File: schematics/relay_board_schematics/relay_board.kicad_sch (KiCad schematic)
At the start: 42 parts, among them J1 Programming Header, P1 ACT_PWR, P2 ACT_PWR, P3 ACTUATOR, Q1 MMBF170, Q2 MMBF170, SW1 SW_DIP_x04, U1 SPST_POWER_RELAY, U2 PIC16F1826-ISO, U3 dpdt_relay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

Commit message: clean up on project files naming except symbol lib
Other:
- title: RLCS Relay_Board -> RLCS Relay Board
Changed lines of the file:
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@@
   (paper "A4")
   (title_block
-    (title "RLCS Relay_Board")
+    (title "RLCS Relay Board")
     (date "2022-11-25")
     (rev "A")

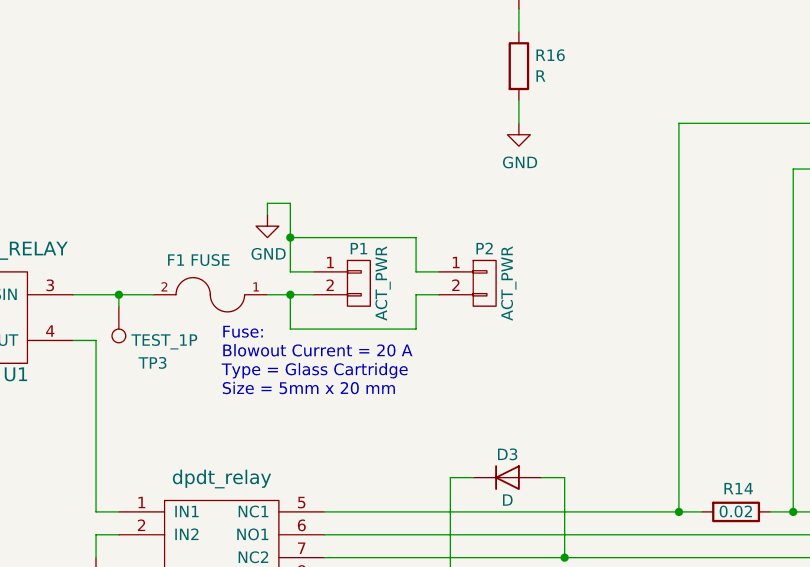
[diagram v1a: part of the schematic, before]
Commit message: reverse pinout on P2 connector
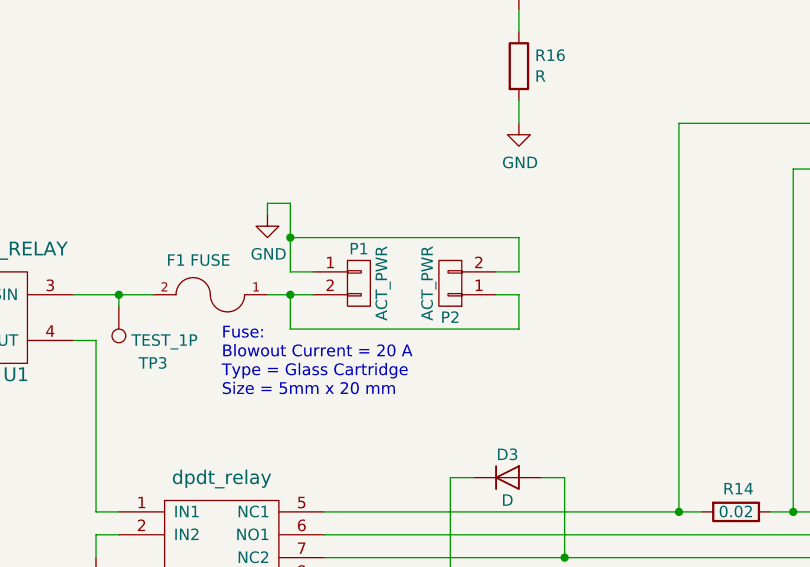
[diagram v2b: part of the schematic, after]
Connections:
- net GND: now also P2.2 (P2); no longer P2.1 (P1)
- net at F1.1, P1.2 (P2): now also P2.1 (P1); no longer P2.2 (P2)
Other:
- moved on the sheet: P2
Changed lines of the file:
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@@
-    (stroke (width 0) (type default) (color 0 0 0 0))
-  )
-  (wire (pts (xy 158.75 120.65) (xy 172.72 120.65))
     (stroke (width 0) (type default) (color 0 0 0 0))
   )
@@
     (stroke (width 0) (type default) (color 0 0 0 0))
   )
+  (wire (pts (xy 184.15 116.84) (xy 181.61 116.84))
+    (stroke (width 0) (type default) (color 0 0 0 0))
+  )
   (wire (pts (xy 218.44 119.38) (xy 233.68 119.38))
     (stroke (width 0) (type default) (color 0 0 0 0))
@@
     (stroke (width 0) (type default) (color 0 0 0 0))
   )
+  (wire (pts (xy 158.75 120.65) (xy 184.15 120.65))
+    (stroke (width 0) (type default) (color 0 0 0 0))
+  )
   (wire (pts (xy 48.006 35.814) (xy 48.006 39.37))
     (stroke (width 0) (type default) (color 0 0 0 0))
@@
     (stroke (width 0) (type default) (color 0 0 0 0))
   )
-  (wire (pts (xy 172.72 116.84) (xy 172.72 120.65))
-    (stroke (width 0) (type default) (color 0 0 0 0))
-  )
   (wire (pts (xy 73.66 86.36) (xy 71.12 86.36))
     (stroke (width 0) (type default) (color 0 0 0 0))
@@
     (stroke (width 0) (type default) (color 0 0 0 0))
   )
+  (wire (pts (xy 184.15 110.49) (xy 184.15 114.3))
+    (stroke (width 0) (type default) (color 0 0 0 0))
+  )
   (wire (pts (xy 212.09 140.97) (xy 214.63 140.97))
     (stroke (width 0) (type default) (color 0 0 0 0))
@@
     (stroke (width 0) (type default) (color 0 0 0 0))
   )
-  (wire (pts (xy 175.26 114.3) (xy 172.72 114.3))
-    (stroke (width 0) (type default) (color 0 0 0 0))
-  )
   (wire (pts (xy 194.31 25.4) (xy 194.31 26.67))
     (stroke (width 0) (type default) (color 0 0 0 0))
@@
     (stroke (width 0) (type default) (color 0 0 0 0))
   )
+  (wire (pts (xy 184.15 120.65) (xy 184.15 116.84))
+    (stroke (width 0) (type default) (color 0 0 0 0))
+  )
   (wire (pts (xy 119.38 186.69) (xy 119.38 184.15))
     (stroke (width 0) (type default) (color 0 0 0 0))
@@
     (stroke (width 0) (type default) (color 0 0 0 0))
   )
+  (wire (pts (xy 184.15 114.3) (xy 181.61 114.3))
+    (stroke (width 0) (type default) (color 0 0 0 0))
+  )
   (wire (pts (xy 201.93 97.79) (xy 201.93 140.97))
     (stroke (width 0) (type default) (color 0 0 0 0))
@@
     (stroke (width 0) (type default) (color 0 0 0 0))
   )
-  (wire (pts (xy 158.75 110.49) (xy 172.72 110.49))
+  (wire (pts (xy 158.75 110.49) (xy 184.15 110.49))
     (stroke (width 0) (type default) (color 0 0 0 0))
   )
@@
     (stroke (width 0) (type default) (color 0 0 0 0))
   )
-  (wire (pts (xy 175.26 116.84) (xy 172.72 116.84))
-    (stroke (width 0) (type default) (color 0 0 0 0))
-  )
   (wire (pts (xy 87.63 39.37) (xy 92.71 39.37))
     (stroke (width 0) (type default) (color 0 0 0 0))
@@
   )
   (wire (pts (xy 189.23 137.16) (xy 189.23 146.05))
-    (stroke (width 0) (type default) (color 0 0 0 0))
-  )
-  (wire (pts (xy 172.72 114.3) (xy 172.72 110.49))
     (stroke (width 0) (type default) (color 0 0 0 0))
   )
@@
     (pin "1")
   )
-  (symbol (lib_id "rlcsv4_modular-rescue:CONN_01X02-rlcsv3_modular-rescue") (at 180.34 115.57 0) (unit 1)
-    (in_bom yes) (on_board yes)
-    (property "Reference" "P2" (id 0) (at 180.34 111.76 0))
-    (property "Value" "ACT_PWR" (id 1) (at 182.88 115.57 90))
-    (property "Footprint" "TerminalBlock_Phoenix:TerminalBlock_Phoenix_MKDS-1,5-2-5.08_1x02_P5.08mm_Horizontal" (id 2) (at 180.34 115.57 0)
-      (effects (font (size 1.27 1.27)) hide)
-    )
-    (property "Datasheet" "" (id 3) (at 180.34 115.57 0))
-    (pin "1")
-    (pin "2")
+  (symbol (lib_id "rlcsv4_modular-rescue:CONN_01X02-rlcsv3_modular-rescue") (at 176.53 115.57 180) (unit 1)
+    (in_bom yes) (on_board yes)
+    (property "Reference" "P2" (id 0) (at 176.53 119.38 0))
+    (property "Value" "ACT_PWR" (id 1) (at 173.99 115.57 90))
+    (property "Footprint" "TerminalBlock_Phoenix:TerminalBlock_Phoenix_MKDS-1,5-2-5.08_1x02_P5.08mm_Horizontal" (id 2) (at 176.53 115.57 0)
+      (effects (font (size 1.27 1.27)) hide)
+    )
+    (property "Datasheet" "" (id 3) (at 176.53 115.57 0))
+    (pin "1")
+    (pin "2")

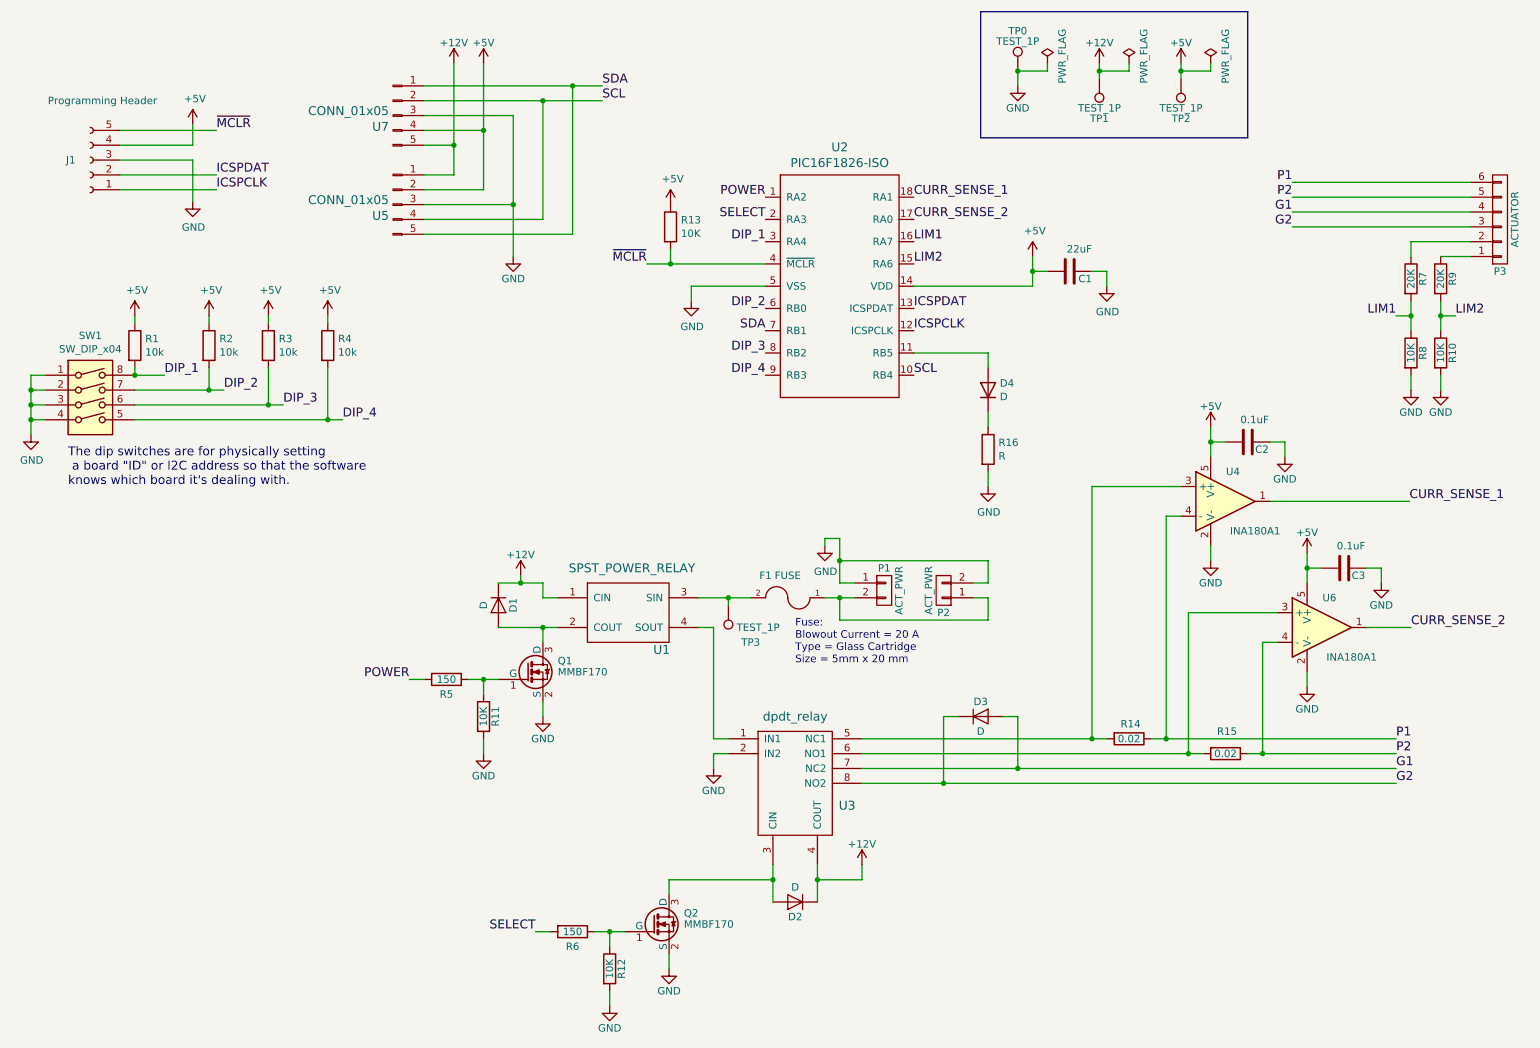
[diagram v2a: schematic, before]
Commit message: Clean up on relay board symbol library name and symbol names and add protection diodes to G1/G2 terminals on actuator header
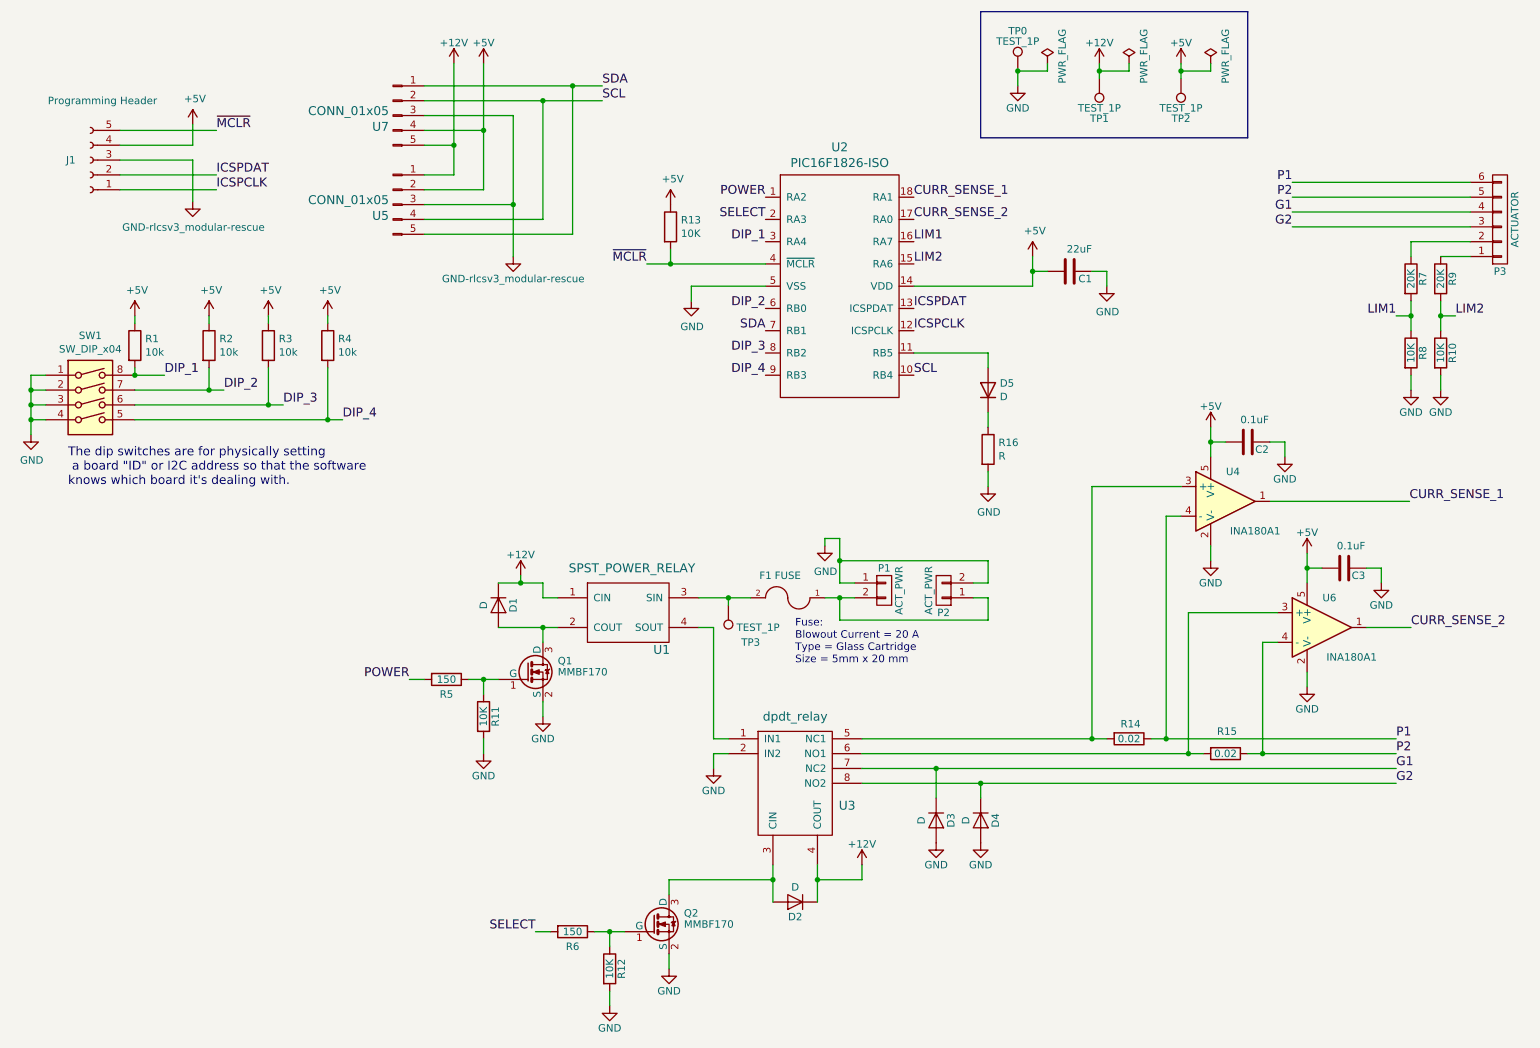
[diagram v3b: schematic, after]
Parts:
- removed D3: D, Diode_THT:D_DO-35_SOD27_P7.62mm_Horizontal, symbol rlcsv4_modular-rescue:D-rlcsv3_modular-rescue
- added D3, D4: D, symbol relay_board:D-rlcs_relay_board
- C1: footprint Capacitor_SMD:C_0805_2012Metric_Pad1.15x1.40mm_HandSolder -> (none)
- C2, C3: footprint Capacitor_SMD:C_0805_2012Metric_Pad1.15x1.40mm_HandSolder -> (none); symbol rlcsv4_modular-rescue:C-rlcsv3_modular-rescue -> relay_board:C-rlcs_relay_board
- D1, D2: footprint Diode_THT:D_DO-35_SOD27_P7.62mm_Horizontal -> (none); symbol rlcsv4_modular-rescue:D-rlcsv3_modular-rescue -> relay_board:D-rlcs_relay_board
- D5: renamed from D4; footprint LED_SMD:LED_1206_3216Metric_Pad1.42x1.75mm_HandSolder -> (none)
- F1: footprint rlcs:littlefuse_01000020Z -> (none); symbol rlcsv4_modular-rescue:FUSE-rlcsv3_modular-rescue -> relay_board:FUSE-rlcs_relay_board
- J1: footprint rlcs:PinHeader_5x2.54_SMD_90deg_952-3198-1-ND -> (none)
- P1, P2: footprint TerminalBlock_Phoenix:TerminalBlock_Phoenix_MKDS-1,5-2-5.08_1x02_P5.08mm_Horizontal -> (none); symbol rlcsv4_modular-rescue:CONN_01X02-rlcsv3_modular-rescue -> relay_board:CONN_01X02-rlcs_relay_board
- P3: footprint TerminalBlock_Phoenix:TerminalBlock_Phoenix_MKDS-1,5-6_1x06_P5.00mm_Horizontal -> (none); symbol rlcsv4_modular-rescue:CONN_01X06-rlcsv3_modular-rescue -> relay_board:CONN_01X06-rlcs_relay_board
- Q1, Q2: symbol rlcsv4_modular-rescue:MMBF170-rlcsv3_modular-rescue -> relay_board:MMBF170-rlcs_relay_board
- R1, R13, R16, R2, R3, R4: footprint Resistor_SMD:R_0805_2012Metric_Pad1.15x1.40mm_HandSolder -> (none)
- R10, R11, R12, R5, R6, R7, R8, R9: footprint Resistor_SMD:R_0805_2012Metric_Pad1.15x1.40mm_HandSolder -> (none); symbol rlcsv4_modular-rescue:R-rlcsv3_modular-rescue -> relay_board:R-rlcs_relay_board
- R14, R15: footprint Resistor_SMD:R_2512_6332Metric_Pad1.52x3.35mm_HandSolder -> (none); symbol rlcsv4_modular-rescue:R-rlcsv3_modular-rescue -> relay_board:R-rlcs_relay_board
- SW1: footprint rlcs:DIP_SWITCH_4X2 -> (none)
- TP0, TP1, TP2, TP3: footprint Socket_Strips:Socket_Strip_Straight_1x01_Pitch2.54mm -> (none); symbol rlcsv4_modular-rescue:TEST_1P-rlcsv3_modular-rescue -> relay_board:TEST_1P-rlcs_relay_board
- U1: footprint rlcs:Relay_SPST_G5LE-1A -> (none); symbol rlcsv4_modular-rescue:SPST_POWER_RELAY-rlcsv3_modular-rescue -> relay_board:SPST_POWER_RELAY-rlcs_relay_board
- U2: footprint rlcs:PIC16F1826-ISO -> (none); symbol rlcsv4_modular-rescue:PIC16F1826-ISO-rlcsv3_modular-rescue -> relay_board:PIC16F1826-ISO-rlcs_relay_board
- U3: footprint rlcs:Relay_DPDT_RT424012F -> (none); symbol rlcsv4_modular-rescue:dpdt_relay-rlcsv3_modular-rescue -> relay_board:dpdt_relay-rlcs_relay_board
- U4, U6: footprint Package_TO_SOT_SMD:SOT-23-5_HandSoldering -> (none); symbol rlcsv4_modular-rescue:MCP601-rlcsv3_modular-rescue -> relay_board:MCP601-rlcs_relay_board
- U5, U7: footprint Connector_JST:JST_XH_S5B-XH-A-1_1x05_P2.50mm_Horizontal -> (none); symbol rlcsv4_modular-rescue:CONN_01x05-rlcsv3_modular-rescue -> relay_board:CONN_01x05-rlcs_relay_board
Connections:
- net G1: now also D3.1 (K)
- net G2: now also D4.1 (K)
- net GND: now also D3.2 (A), D4.2 (A)

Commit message: Filled in missing R16 value, updated D5 symbol, added optional diodes D6/D7
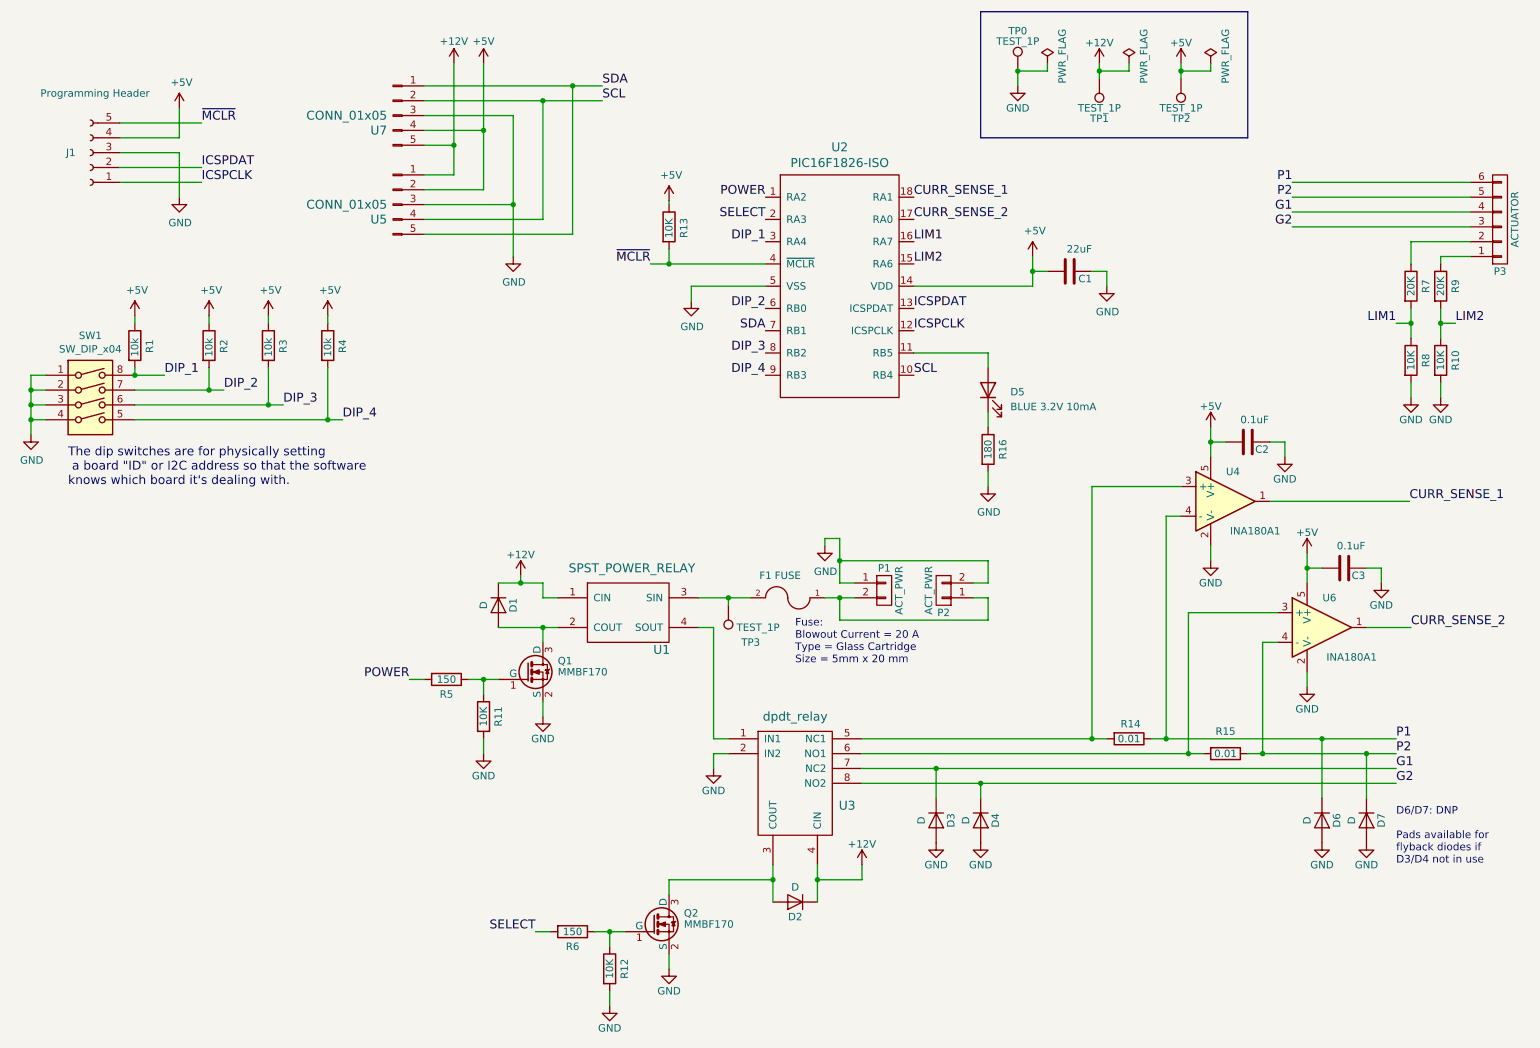
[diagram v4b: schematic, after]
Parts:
- removed D5: D, symbol Device:D
- removed R16: R, symbol Device:R
- added D5: BLUE 3.2V 10mA, LED_THT:LED_D5.0mm_Clear, symbol Device:LED
- added D6, D7: D, Diode_SMD:D_SMB_Handsoldering, symbol relay_board:D-rlcs_relay_board
- added R16: 180, symbol relay_board:R-rlcs_relay_board
- D1, D2, D3, D4: footprint (none) -> Diode_SMD:D_SMB_Handsoldering
- R14, R15: value 0.02 -> 0.01
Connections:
- net GND: now also D6.2 (A), D7.2 (A), R16.2
- net P1: now also D6.1 (K)
- net P2: now also D7.1 (K)
- net at U2.11 (RB5): now also D5.2 (A)
- new net: D5.1 (K), R16.1
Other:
- note added: "D6/D7: DNP Pads available for flyback diodes if D3/D4 not in use"
- moved on the sheet: J1, R10, R7, R8, R9

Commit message: added footprints to all components
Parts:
- C1, C2, C3: footprint (none) -> Capacitor_SMD:C_0805_2012Metric_Pad1.18x1.45mm_HandSolder
- D5: footprint LED_THT:LED_D5.0mm_Clear -> LED_SMD:LED_1206_3216Metric_Pad1.42x1.75mm_HandSolder
- F1: footprint (none) -> custom:littlefuse_01000020Z
- J1: footprint (none) -> custom:PinHeader_5x2.54_SMD_90deg_952-3198-1-ND
- P1, P2: footprint (none) -> TerminalBlock_Phoenix:TerminalBlock_Phoenix_MKDS-1,5-2-5.08_1x02_P5.08mm_Horizontal
- P3: footprint (none) -> TerminalBlock_Phoenix:TerminalBlock_Phoenix_MKDS-1,5-6_1x06_P5.00mm_Horizontal
- Q1, Q2: footprint TO_SOT_Packages_SMD:SOT-23 -> Package_TO_SOT_SMD:SOT-23_Handsoldering
- R1, R10, R11, R12, R13, R16, R2, R3, R4, R5, R6, R7, R8, R9: footprint (none) -> Resistor_SMD:R_0805_2012Metric_Pad1.20x1.40mm_HandSolder
- R14, R15: footprint (none) -> Resistor_SMD:R_2512_6332Metric_Pad1.40x3.35mm_HandSolder
- SW1: footprint (none) -> custom:DIP_SWITCH_4X2
- TP0, TP1, TP2, TP3: footprint (none) -> TestPoint:TestPoint_Loop_D2.50mm_Drill1.0mm_LowProfile
- U1: footprint (none) -> custom:Relay_SPST_G5LE-1A
- U2: footprint (none) -> custom:PIC16F1826-ISO
- U3: footprint (none) -> custom:Relay_DPDT_RT424012F
- U4, U6: footprint (none) -> Package_TO_SOT_SMD:SOT-23-5_HandSoldering
- U5, U7: footprint (none) -> Connector_JST:JST_XH_S5B-XH-A-1_1x05_P2.50mm_Horizontal
